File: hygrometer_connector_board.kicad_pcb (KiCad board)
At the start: 2 copper layers, 92 x 26 mm, 10 parts, among them J1 AudioJack3_SwitchTR, J10 POWER_EN, J2 AudioJack3_SwitchTR, J3 AudioJack3_SwitchTR, J4 AudioJack3_SwitchTR, J5 AudioJack3_SwitchTR, J6 AudioJack3_SwitchTR, J7 AudioJack3_SwitchTR, J8 ANALOG_OUT, J9 POWER_IN

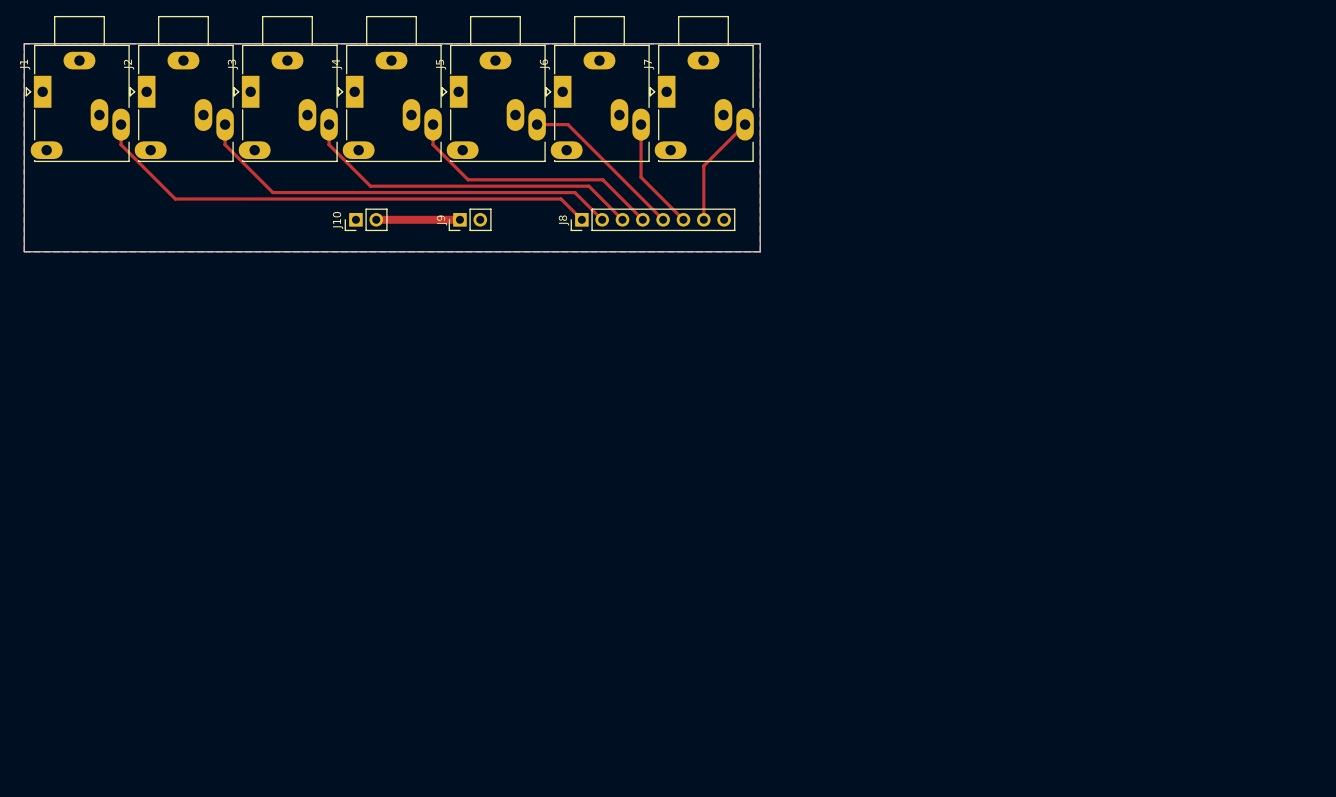
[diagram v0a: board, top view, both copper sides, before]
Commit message: Rev 1.0 done, pending dimension check
- Redrew audio jack footprint
- Mirrored audio jack footprints to back of board
- Resized board and repositioned audio jack footprints
- Switched to right-angle headers
- Ground and power plane on top layer
- Added flower artwork
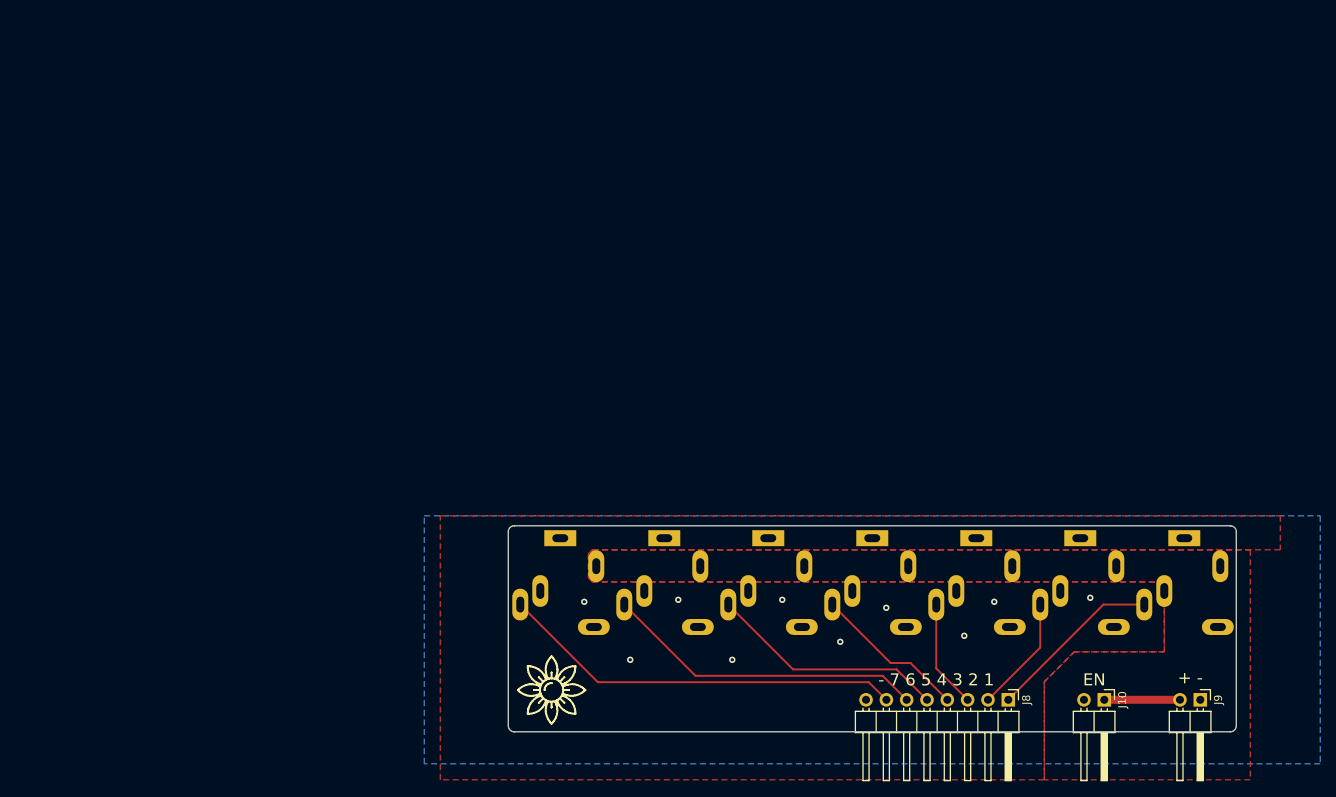
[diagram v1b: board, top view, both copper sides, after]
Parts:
- added REF**: flower, hygrometer_connector_board:flower, F.Cu at (106.0, 120.5)
- J1, J2, J3, J4, J5, J6, J7: value AudioJack3_SwitchTR -> SJ1-3515; footprint Connector_Audio:Jack_3.5mm_Ledino_KB3SPRS_Horizontal -> hygrometer_connector_board:Jack_3.5mm_CUI_SJ1-3515; moved to B.Cu
- J10, J9: footprint Connector_PinHeader_2.54mm:PinHeader_1x02_P2.54mm_Vertical -> Connector_PinHeader_2.54mm:PinHeader_1x02_P2.54mm_Horizontal
- J8: footprint Connector_PinHeader_2.54mm:PinHeader_1x08_P2.54mm_Vertical -> Connector_PinHeader_2.54mm:PinHeader_1x08_P2.54mm_Horizontal
- moved J1 153.2 mm to (185.0, 101.8)
- moved J2 129.4 mm to (172.0, 101.8)
- moved J10 111.1 mm to (175.0, 122.0), turned to 270 degrees
- moved J9 110.3 mm to (187.0, 122.0), turned to 270 degrees
- moved J3 106.5 mm to (159.0, 101.8)
- moved J4 85.4 mm to (146.0, 101.8)
- moved J8 80.3 mm to (163.0, 122.0), turned to 270 degrees
- moved J5 67.9 mm to (133.0, 101.8)
- moved J7 57.4 mm to (107.0, 101.8)
- moved J6 57.2 mm to (120.0, 101.8)
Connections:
- J1 pad RN: Net-(J1-PadRN) -> (no net)
- J1 pad T: +5V -> VCC
- J1 pad TN: Net-(J1-PadTN) -> (no net)
- J10 pad 1: +5V -> Net-(J10-Pad1)
- J10 pad 2: Net-(J10-Pad2) -> VCC
- J2 pad RN: Net-(J2-PadRN) -> (no net)
- J2 pad T: +5V -> VCC
- J2 pad TN: Net-(J2-PadTN) -> (no net)
- J3 pad RN: Net-(J3-PadRN) -> (no net)
- J3 pad T: +5V -> VCC
- J3 pad TN: Net-(J3-PadTN) -> (no net)
- J4 pad RN: Net-(J4-PadRN) -> (no net)
- J4 pad T: +5V -> VCC
- J4 pad TN: Net-(J4-PadTN) -> (no net)
- J5 pad RN: Net-(J5-PadRN) -> (no net)
- J5 pad T: +5V -> VCC
- J5 pad TN: Net-(J5-PadTN) -> (no net)
- J6 pad RN: Net-(J6-PadRN) -> (no net)
- J6 pad T: +5V -> VCC
- J6 pad TN: Net-(J6-PadTN) -> (no net)
- J7 pad RN: Net-(J7-PadRN) -> (no net)
- J7 pad T: +5V -> VCC
- J7 pad TN: Net-(J7-PadTN) -> (no net)
- J9 pad 1: Net-(J10-Pad2) -> GND
- J9 pad 2: GND -> Net-(J10-Pad1)
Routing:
- net /CH1: track 64.0 -> 21.9 mm
- net /CH2: track 53.5 -> 14.6 mm
- net /CH7: track 14.0 -> 50.7 mm
- net /CH3: track 43.1 -> 13.5 mm
- net /CH6: track 14.1 -> 40.2 mm
- net /CH4: track 32.6 -> 19.3 mm
- net Net-(J10-Pad2): track 10.5 -> 0.00 mm
- net Net-(J10-Pad1): track 0.00 -> 9.46 mm
- net /CH5: track 20.7 -> 29.8 mm
- net GND: vias 0 -> 10
- added copper zone on F.Cu, net GND
- added copper zone on F.Cu, net VCC
- removed copper zone on F.Cu, net +5V
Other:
- board size 92 x 26 mm -> 91 x 25.8 mm
- board text added: "+ -"
- board text added: "- 7 6 5 4 3 2 1"
- board text added: "Board dimensions"
- board text added: "EN"
- board text added: "Outline of 3d printed pocket behind sensor jack panel"
- board text removed: "TODO: Mirror audio jack footprints"
